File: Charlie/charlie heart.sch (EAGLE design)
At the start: 33 parts, among them Q1 BSS84

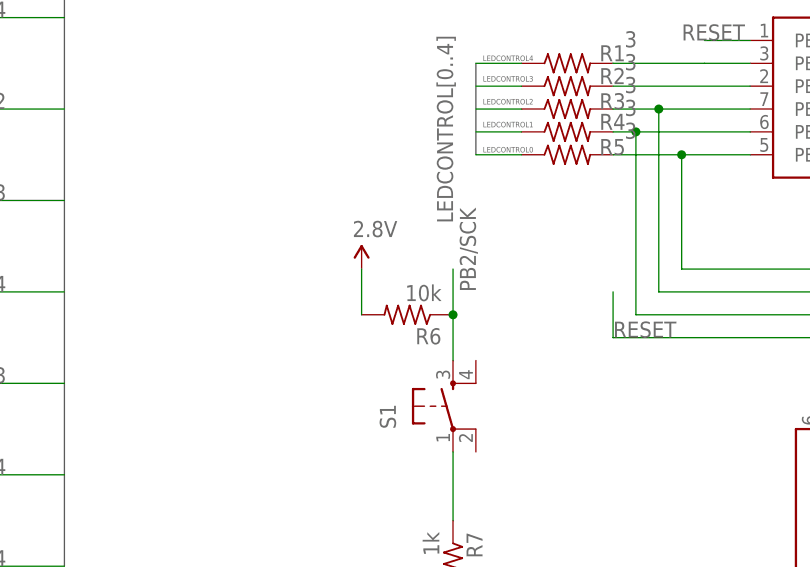
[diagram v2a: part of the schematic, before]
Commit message: remove pullup resistor
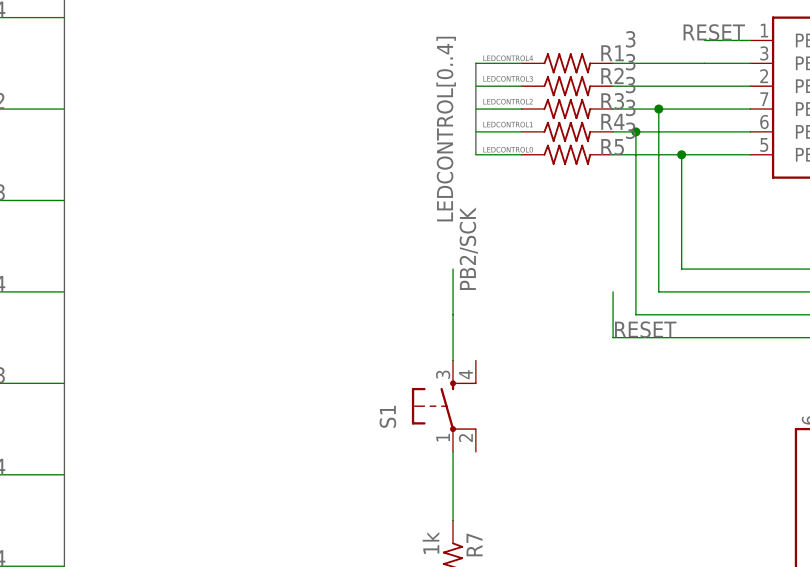
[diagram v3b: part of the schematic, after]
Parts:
- removed R6: 10k, rcl:R-US_R0805
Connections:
- net 2.8V: no longer R6.2
- net PB2/SCK: no longer R6.1
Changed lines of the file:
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@@
 <part name="SUPPLY2" library="SparkFun-Aesthetics" deviceset="2.8V" device=""/>
 <part name="S1" library="SparkFun" deviceset="TAC_SWITCH" device="SMD"/>
-<part name="R6" library="rcl" deviceset="R-US_" device="R0805" value="10k"/>
 <part name="R7" library="rcl" deviceset="R-US_" device="R0805" value="1k"/>
-<part name="SUPPLY3" library="SparkFun-Aesthetics" deviceset="2.8V" device=""/>
 <part name="GND2" library="SparkFun-Aesthetics" deviceset="GND" device=""/>
 </parts>
@@
 <instance part="SUPPLY2" gate="G$1" x="248.92" y="48.26"/>
 <instance part="S1" gate="S" x="180.34" y="17.78" rot="R90"/>
-<instance part="R6" gate="G$1" x="175.26" y="27.94" rot="R180"/>
 <instance part="R7" gate="G$1" x="180.34" y="0" rot="R270"/>
-<instance part="SUPPLY3" gate="G$1" x="170.18" y="33.02"/>
 <instance part="GND2" gate="1" x="180.34" y="-7.62"/>
 </instances>
@@
 <pinref part="S1" gate="S" pin="3"/>
 <wire x1="180.34" y1="22.86" x2="180.34" y2="27.94" width="0.1524" layer="91"/>
-<pinref part="R6" gate="G$1" pin="1"/>
 <wire x1="180.34" y1="27.94" x2="180.34" y2="33.02" width="0.1524" layer="91"/>
-<junction x="180.34" y="27.94"/>
 <label x="182.88" y="30.48" size="1.778" layer="95" rot="R90"/>
 </segment>
@@
 <pinref part="SUPPLY2" gate="G$1" pin="2.8V"/>
 </segment>
-<segment>
-<pinref part="R6" gate="G$1" pin="2"/>
-<wire x1="170.18" y1="27.94" x2="170.18" y2="33.02" width="0.1524" layer="91"/>
-<pinref part="SUPPLY3" gate="G$1" pin="2.8V"/>
-</segment>
-</net>
+</net>

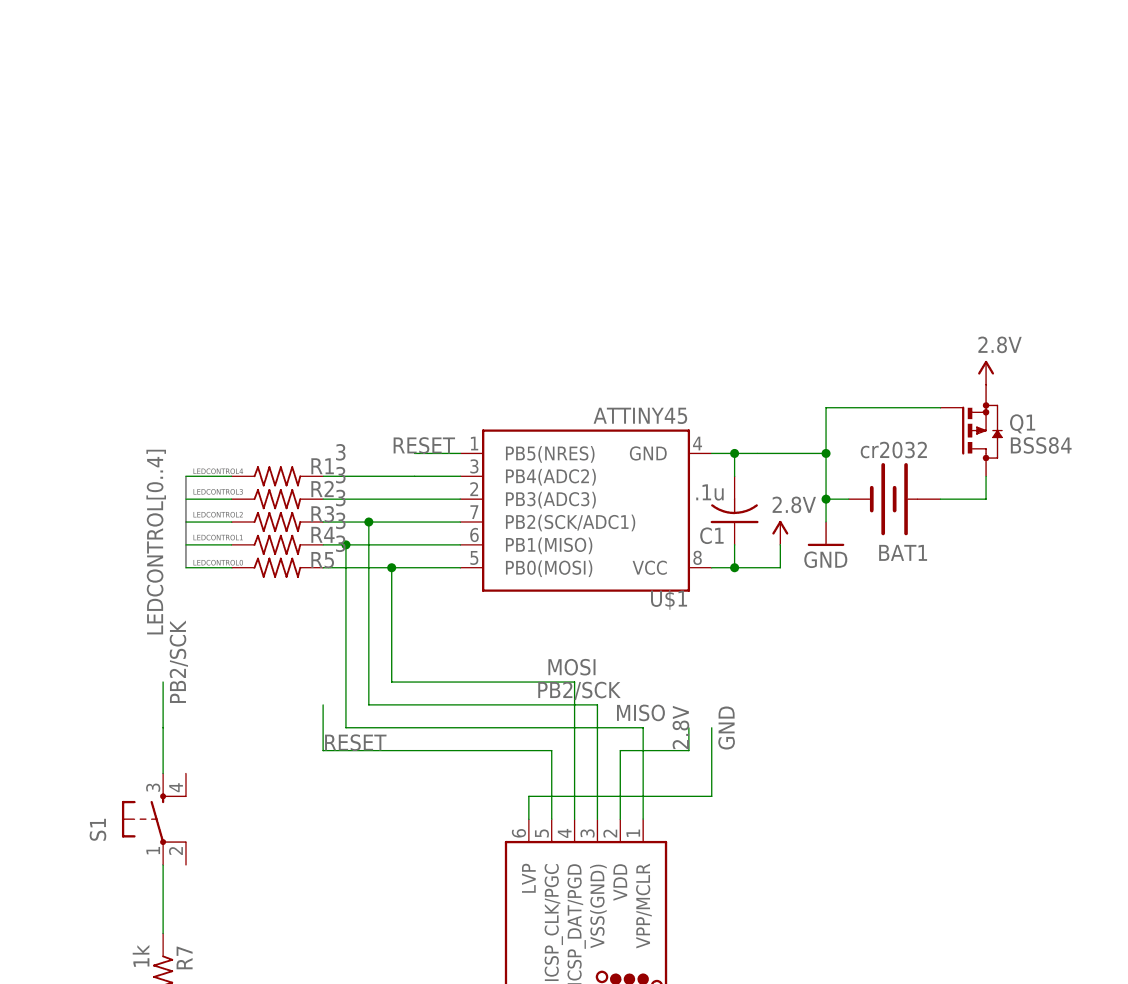
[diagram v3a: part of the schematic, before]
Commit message: new board with tiny841
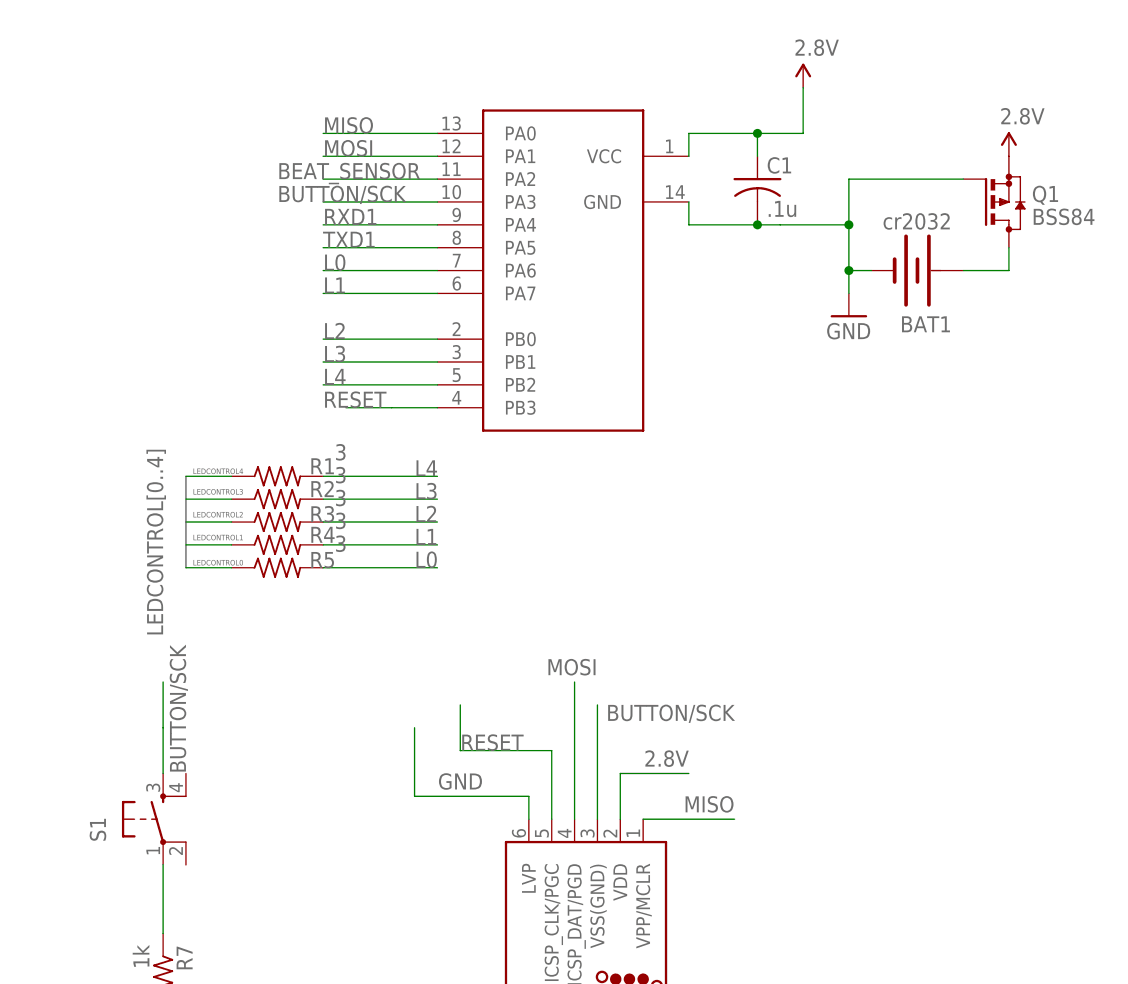
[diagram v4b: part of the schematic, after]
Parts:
- removed U$1: ATTINY45, SparkFun:ATTINY45
- added U1: ATTINY841, Atmel_By_element14_Batch_1-00:ATTINY841-SSU
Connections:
- removed net N$4: R2.2, U$1.PB3(ADC3)
- removed net N$6: R1.2, U$1.PB4(ADC2)
- removed net PB2/SCK: J1.VSS(GND), R3.2, S1.3, U$1.PB2(SCK/ADC1)
- new net BEAT_SENSOR: U1.PA2
- new net BUTTON/SCK: J1.VSS(GND), S1.3, U1.PA3
- new net L0: R5.2, U1.PA6
- new net L1: R4.2, U1.PA7
- new net L2: R3.2, U1.PB0
- new net L3: R2.2, U1.PB1
- new net L4: R1.2, U1.PB2
- new net RXD1: U1.PA4
- new net TXD1: U1.PA5
- net 2.8V: now also U1.VCC; no longer U$1.VCC
- net GND: now also U1.GND; no longer U$1.GND
- net MISO: now also U1.PA0; no longer R4.2, U$1.PB1(MISO)
- net MOSI: now also U1.PA1; no longer R5.2, U$1.PB0(MOSI)
- net RESET: now also U1.PB3; no longer U$1.PB5(NRES)
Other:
- moved on the sheet: BAT1, C1, Q1

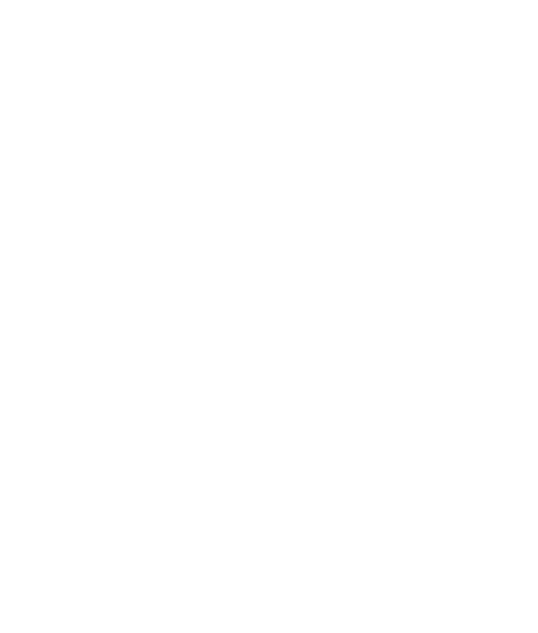
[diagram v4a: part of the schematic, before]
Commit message: add jumpers for serial and beat sensor
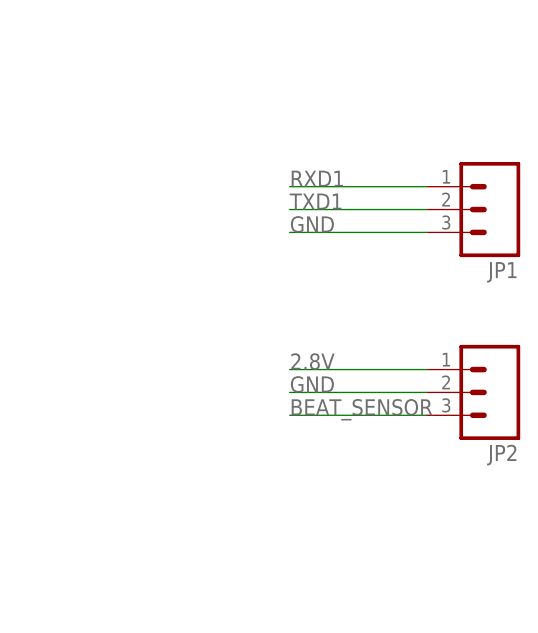
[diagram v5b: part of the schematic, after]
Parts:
- added JP1, JP2: (no value), SparkFun:M031X03_NO_SILK
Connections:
- net 2.8V: now also JP2.1
- net BEAT_SENSOR: now also JP2.3
- net GND: now also JP1.3, JP2.2
- net RXD1: now also JP1.1
- net TXD1: now also JP1.2
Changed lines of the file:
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@@
 <part name="GND2" library="SparkFun-Aesthetics" deviceset="GND" device=""/>
 <part name="U1" library="Atmel_By_element14_Batch_1-00" deviceset="ATTINY841-SSU" device="" value="ATTINY841"/>
+<part name="JP2" library="SparkFun" deviceset="M03" device="1X03_NO_SILK"/>
+<part name="JP1" library="SparkFun" deviceset="M03" device="1X03_NO_SILK"/>
 </parts>
 <sheets>
@@
 <instance part="GND2" gate="1" x="180.34" y="-7.62"/>
 <instance part="U1" gate="G$1" x="228.6" y="76.2"/>
+<instance part="JP2" gate="G$1" x="307.34" y="25.4" rot="R180"/>
+<instance part="JP1" gate="G$1" x="307.34" y="45.72" rot="R180"/>
 </instances>
 <busses>
@@
 <pinref part="GND2" gate="1" pin="GND"/>
 </segment>
+<segment>
+<pinref part="JP1" gate="G$1" pin="3"/>
+<wire x1="299.72" y1="43.18" x2="284.48" y2="43.18" width="0.1524" layer="91"/>
+<label x="284.48" y="43.18" size="1.778" layer="95"/>
+</segment>
+<segment>
+<pinref part="JP2" gate="G$1" pin="2"/>
+<wire x1="299.72" y1="25.4" x2="284.48" y2="25.4" width="0.1524" layer="91"/>
+<label x="284.48" y="25.4" size="1.778" layer="95"/>
+</segment>
 </net>
 <net name="2.8V" class="1">
@@
 <junction x="246.38" y="93.98"/>
 </segment>
+<segment>
+<pinref part="JP2" gate="G$1" pin="1"/>
+<wire x1="299.72" y1="27.94" x2="284.48" y2="27.94" width="0.1524" layer="91"/>
+<label x="284.48" y="27.94" size="1.778" layer="95"/>
+</segment>
 </net>
 <net name="RESET" class="0">
@@
 <label x="198.12" y="83.82" size="1.778" layer="95"/>
 </segment>
+<segment>
+<pinref part="JP1" gate="G$1" pin="1"/>
+<wire x1="299.72" y1="48.26" x2="284.48" y2="48.26" width="0.1524" layer="91"/>
+<label x="284.48" y="48.26" size="1.778" layer="95"/>
+</segment>
 </net>
 <net name="TXD1" class="0">
@@
 <label x="198.12" y="81.28" size="1.778" layer="95"/>
 </segment>
+<segment>
+<pinref part="JP1" gate="G$1" pin="2"/>
+<wire x1="299.72" y1="45.72" x2="284.48" y2="45.72" width="0.1524" layer="91"/>
+<label x="284.48" y="45.72" size="1.778" layer="95"/>
+</segment>
 </net>
 <net name="L0" class="0">
@@
 <label x="193.04" y="88.9" size="1.778" layer="95"/>
 </segment>
-</net>
+<segment>
+<pinref part="JP2" gate="G$1" pin="3"/>
+<wire x1="299.72" y1="22.86" x2="284.48" y2="22.86" width="0.1524" layer="91"/>
+<label x="284.48" y="22.86" size="1.778" layer="95"/>
+</segment>
+</net>

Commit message: update program lines
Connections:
- removed net BUTTON/SCK: J1.VSS(GND), S1.3, U1.PA3
- removed net L2: R3.2, U1.PB0
- removed net RXD1: JP1.1, U1.PA4
- removed net TXD1: JP1.2, U1.PA5
- new net BUTTON: S1.3, U1.PA3
- new net RXD0: JP1.1, U1.PB2
- new net SCK/L2: J1.VSS(GND), R3.2, U1.PA4
- new net TXD0: JP1.2, U1.PA7
- net L0: now also U1.PA0; no longer U1.PA6
- net L1: now also U1.PA1; no longer U1.PA7
- net L3: now also U1.PB0; no longer U1.PB1
- net L4: now also U1.PB1; no longer U1.PB2
- net MISO: now also U1.PA5; no longer U1.PA0
- net MOSI: now also U1.PA6; no longer U1.PA1
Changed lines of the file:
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@@
 </segment>
 <segment>
-<pinref part="U1" gate="G$1" pin="PA1"/>
-<wire x1="210.82" y1="91.44" x2="198.12" y2="91.44" width="0.1524" layer="91"/>
-<label x="198.12" y="91.44" size="1.778" layer="95"/>
+<pinref part="U1" gate="G$1" pin="PA6"/>
+<wire x1="210.82" y1="78.74" x2="198.12" y2="78.74" width="0.1524" layer="91"/>
+<label x="198.12" y="78.74" size="1.778" layer="95"/>
 </segment>
 </net>
@@
 </segment>
 <segment>
-<pinref part="U1" gate="G$1" pin="PA0"/>
-<wire x1="210.82" y1="93.98" x2="198.12" y2="93.98" width="0.1524" layer="91"/>
-<label x="198.12" y="93.98" size="1.778" layer="95"/>
-</segment>
-</net>
-<net name="BUTTON/SCK" class="0">
-<segment>
-<pinref part="S1" gate="S" pin="3"/>
-<wire x1="180.34" y1="22.86" x2="180.34" y2="27.94" width="0.1524" layer="91"/>
-<wire x1="180.34" y1="27.94" x2="180.34" y2="33.02" width="0.1524" layer="91"/>
-<label x="182.88" y="22.86" size="1.778" layer="95" rot="R90"/>
-</segment>
-<segment>
-<pinref part="U1" gate="G$1" pin="PA3"/>
-<wire x1="210.82" y1="86.36" x2="198.12" y2="86.36" width="0.1524" layer="91"/>
-<label x="193.04" y="86.36" size="1.778" layer="95"/>
-</segment>
-<segment>
-<pinref part="J1" gate="G$1" pin="VSS(GND)"/>
-<wire x1="228.6" y1="17.78" x2="228.6" y2="30.48" width="0.1524" layer="91"/>
-<label x="243.84" y="30.48" size="1.778" layer="95" rot="R180"/>
+<pinref part="U1" gate="G$1" pin="PA5"/>
+<wire x1="210.82" y1="81.28" x2="198.12" y2="81.28" width="0.1524" layer="91"/>
+<label x="198.12" y="81.28" size="1.778" layer="95"/>
 </segment>
 </net>
@@
 <net name="RESET" class="0">
 <segment>
-<wire x1="200.66" y1="63.5" x2="205.74" y2="63.5" width="0.1524" layer="91"/>
+<wire x1="198.12" y1="63.5" x2="205.74" y2="63.5" width="0.1524" layer="91"/>
 <label x="198.12" y="63.5" size="1.778" layer="95"/>
 <pinref part="U1" gate="G$1" pin="PB3"/>
@@
 </segment>
 </net>
-<net name="N$2" class="0">
+<net name="N$2" class="1">
 <segment>
 <wire x1="269.24" y1="78.74" x2="274.32" y2="78.74" width="0.1524" layer="91"/>
@@
 </segment>
 </net>
-<net name="RXD1" class="0">
+<net name="L0" class="0">
+<segment>
+<pinref part="R5" gate="G$1" pin="2"/>
+<wire x1="198.12" y1="45.72" x2="210.82" y2="45.72" width="0.1524" layer="91"/>
+<label x="208.28" y="45.72" size="1.778" layer="95"/>
+</segment>
+<segment>
+<pinref part="U1" gate="G$1" pin="PA0"/>
+<wire x1="210.82" y1="93.98" x2="198.12" y2="93.98" width="0.1524" layer="91"/>
+<label x="198.12" y="93.98" size="1.778" layer="95"/>
+</segment>
+</net>
+<net name="L1" class="0">
+<segment>
+<pinref part="R4" gate="G$1" pin="2"/>
+<wire x1="198.12" y1="48.26" x2="210.82" y2="48.26" width="0.1524" layer="91"/>
+<label x="208.28" y="48.26" size="1.778" layer="95"/>
+</segment>
+<segment>
+<pinref part="U1" gate="G$1" pin="PA1"/>
+<wire x1="210.82" y1="91.44" x2="198.12" y2="91.44" width="0.1524" layer="91"/>
+<label x="198.12" y="91.44" size="1.778" layer="95"/>
+</segment>
+</net>
+<net name="L3" class="0">
+<segment>
+<pinref part="R2" gate="G$1" pin="2"/>
+<wire x1="198.12" y1="53.34" x2="210.82" y2="53.34" width="0.1524" layer="91"/>
+<label x="208.28" y="53.34" size="1.778" layer="95"/>
+</segment>
+<segment>
+<pinref part="U1" gate="G$1" pin="PB0"/>
+<wire x1="210.82" y1="71.12" x2="198.12" y2="71.12" width="0.1524" layer="91"/>
+<label x="198.12" y="71.12" size="1.778" layer="95"/>
+</segment>
+</net>
+<net name="L4" class="0">
+<segment>
+<pinref part="R1" gate="G$1" pin="2"/>
+<wire x1="198.12" y1="55.88" x2="210.82" y2="55.88" width="0.1524" layer="91"/>
+<label x="208.28" y="55.88" size="1.778" layer="95"/>
+</segment>
+<segment>
+<pinref part="U1" gate="G$1" pin="PB1"/>
+<wire x1="210.82" y1="68.58" x2="198.12" y2="68.58" width="0.1524" layer="91"/>
+<label x="198.12" y="68.58" size="1.778" layer="95"/>
+</segment>
+</net>
+<net name="BEAT_SENSOR" class="0">
+<segment>
+<pinref part="U1" gate="G$1" pin="PA2"/>
+<wire x1="210.82" y1="88.9" x2="198.12" y2="88.9" width="0.1524" layer="91"/>
+<label x="193.04" y="88.9" size="1.778" layer="95"/>
+</segment>
+<segment>
+<pinref part="JP2" gate="G$1" pin="3"/>
+<wire x1="299.72" y1="22.86" x2="284.48" y2="22.86" width="0.1524" layer="91"/>
+<label x="284.48" y="22.86" size="1.778" layer="95"/>
+</segment>
+</net>
+<net name="BUTTON" class="0">
+<segment>
+<pinref part="U1" gate="G$1" pin="PA3"/>
+<wire x1="210.82" y1="86.36" x2="198.12" y2="86.36" width="0.1524" layer="91"/>
+<label x="198.12" y="86.36" size="1.778" layer="95"/>
+</segment>
+<segment>
+<pinref part="S1" gate="S" pin="3"/>
+<wire x1="180.34" y1="22.86" x2="180.34" y2="27.94" width="0.1524" layer="91"/>
+<wire x1="180.34" y1="27.94" x2="180.34" y2="33.02" width="0.1524" layer="91"/>
+<label x="182.88" y="22.86" size="1.778" layer="95" rot="R90"/>
+</segment>
+</net>
+<net name="SCK/L2" class="0">
+<segment>
+<pinref part="J1" gate="G$1" pin="VSS(GND)"/>
+<wire x1="228.6" y1="17.78" x2="228.6" y2="30.48" width="0.1524" layer="91"/>
+<label x="241.3" y="33.02" size="1.778" layer="95" rot="R180"/>
+<wire x1="228.6" y1="30.48" x2="233.68" y2="30.48" width="0.1524" layer="91"/>
+</segment>
 <segment>
 <pinref part="U1" gate="G$1" pin="PA4"/>
@@
 </segment>
 <segment>
+<pinref part="R3" gate="G$1" pin="2"/>
+<wire x1="198.12" y1="50.8" x2="210.82" y2="50.8" width="0.1524" layer="91"/>
+<label x="208.28" y="50.8" size="1.778" layer="95"/>
+</segment>
+</net>
+<net name="TXD0" class="0">
+<segment>
+<pinref part="U1" gate="G$1" pin="PA7"/>
+<wire x1="210.82" y1="76.2" x2="198.12" y2="76.2" width="0.1524" layer="91"/>
+<label x="198.12" y="76.2" size="1.778" layer="95"/>
+</segment>
+<segment>
+<pinref part="JP1" gate="G$1" pin="2"/>
+<wire x1="299.72" y1="45.72" x2="284.48" y2="45.72" width="0.1524" layer="91"/>
+<label x="284.48" y="45.72" size="1.778" layer="95"/>
+</segment>
+</net>
+<net name="RXD0" class="0">
+<segment>
+<pinref part="U1" gate="G$1" pin="PB2"/>
+<wire x1="210.82" y1="66.04" x2="198.12" y2="66.04" width="0.1524" layer="91"/>
+<label x="198.12" y="66.04" size="1.778" layer="95"/>
+</segment>
+<segment>
 <pinref part="JP1" gate="G$1" pin="1"/>
 <wire x1="299.72" y1="48.26" x2="284.48" y2="48.26" width="0.1524" layer="91"/>
@@
 </segment>
 </net>
-<net name="TXD1" class="0">
-<segment>
-<pinref part="U1" gate="G$1" pin="PA5"/>
-<wire x1="210.82" y1="81.28" x2="198.12" y2="81.28" width="0.1524" layer="91"/>
-<label x="198.12" y="81.28" size="1.778" layer="95"/>
-</segment>
-<segment>
-<pinref part="JP1" gate="G$1" pin="2"/>
-<wire x1="299.72" y1="45.72" x2="284.48" y2="45.72" width="0.1524" layer="91"/>
-<label x="284.48" y="45.72" size="1.778" layer="95"/>
-</segment>
-</net>
-<net name="L0" class="0">
-<segment>
-<pinref part="U1" gate="G$1" pin="PA6"/>
-<wire x1="210.82" y1="78.74" x2="198.12" y2="78.74" width="0.1524" layer="91"/>
-<label x="198.12" y="78.74" size="1.778" layer="95"/>
-</segment>
-<segment>
-<pinref part="R5" gate="G$1" pin="2"/>
-<wire x1="198.12" y1="45.72" x2="210.82" y2="45.72" width="0.1524" layer="91"/>
-<label x="208.28" y="45.72" size="1.778" layer="95"/>
-</segment>
-</net>
-<net name="L1" class="0">
-<segment>
-<pinref part="U1" gate="G$1" pin="PA7"/>
-<wire x1="210.82" y1="76.2" x2="198.12" y2="76.2" width="0.1524" layer="91"/>
-<label x="198.12" y="76.2" size="1.778" layer="95"/>
-</segment>
-<segment>
-<pinref part="R4" gate="G$1" pin="2"/>
-<wire x1="198.12" y1="48.26" x2="210.82" y2="48.26" width="0.1524" layer="91"/>
-<label x="208.28" y="48.26" size="1.778" layer="95"/>
-</segment>
-</net>
-<net name="L2" class="0">
-<segment>
-<pinref part="U1" gate="G$1" pin="PB0"/>
-<wire x1="210.82" y1="71.12" x2="198.12" y2="71.12" width="0.1524" layer="91"/>
-<label x="198.12" y="71.12" size="1.778" layer="95"/>
-</segment>
-<segment>
-<pinref part="R3" gate="G$1" pin="2"/>
-<wire x1="198.12" y1="50.8" x2="210.82" y2="50.8" width="0.1524" layer="91"/>
-<label x="208.28" y="50.8" size="1.778" layer="95"/>
-</segment>
-</net>
-<net name="L3" class="0">
-<segment>
-<pinref part="U1" gate="G$1" pin="PB1"/>
-<wire x1="210.82" y1="68.58" x2="198.12" y2="68.58" width="0.1524" layer="91"/>
-<label x="198.12" y="68.58" size="1.778" layer="95"/>
-</segment>
-<segment>
-<pinref part="R2" gate="G$1" pin="2"/>
-<wire x1="198.12" y1="53.34" x2="210.82" y2="53.34" width="0.1524" layer="91"/>
-<label x="208.28" y="53.34" size="1.778" layer="95"/>
-</segment>
-</net>
-<net name="L4" class="0">
-<segment>
-<pinref part="U1" gate="G$1" pin="PB2"/>
-<wire x1="210.82" y1="66.04" x2="198.12" y2="66.04" width="0.1524" layer="91"/>
-<label x="198.12" y="66.04" size="1.778" layer="95"/>
-</segment>
-<segment>
-<pinref part="R1" gate="G$1" pin="2"/>
-<wire x1="198.12" y1="55.88" x2="210.82" y2="55.88" width="0.1524" layer="91"/>
-<label x="208.28" y="55.88" size="1.778" layer="95"/>
-</segment>
-</net>
-<net name="BEAT_SENSOR" class="0">
-<segment>
-<pinref part="U1" gate="G$1" pin="PA2"/>
-<wire x1="210.82" y1="88.9" x2="198.12" y2="88.9" width="0.1524" layer="91"/>
-<label x="193.04" y="88.9" size="1.778" layer="95"/>
-</segment>
-<segment>
-<pinref part="JP2" gate="G$1" pin="3"/>
-<wire x1="299.72" y1="22.86" x2="284.48" y2="22.86" width="0.1524" layer="91"/>
-<label x="284.48" y="22.86" size="1.778" layer="95"/>
-</segment>
-</net>
